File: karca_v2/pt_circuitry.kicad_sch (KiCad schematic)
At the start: 12 parts, among them U10 TLV9304xD, U9 TLV9304xD

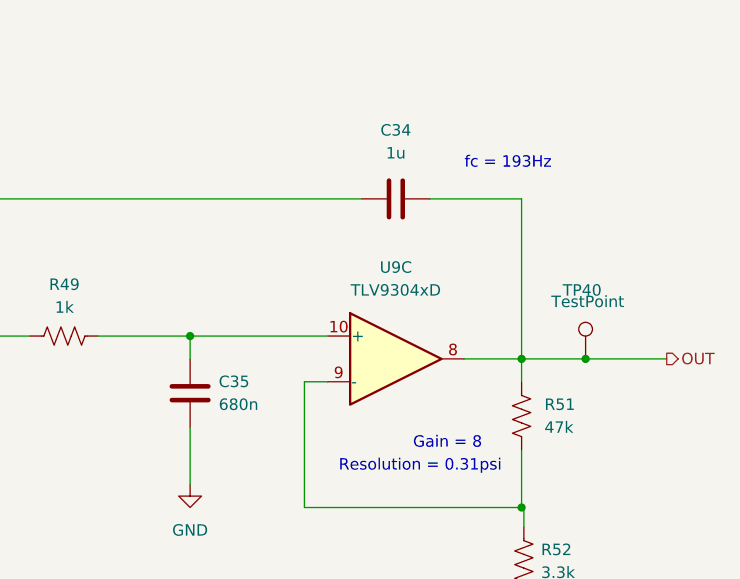
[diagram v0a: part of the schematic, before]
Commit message: swapped adcs
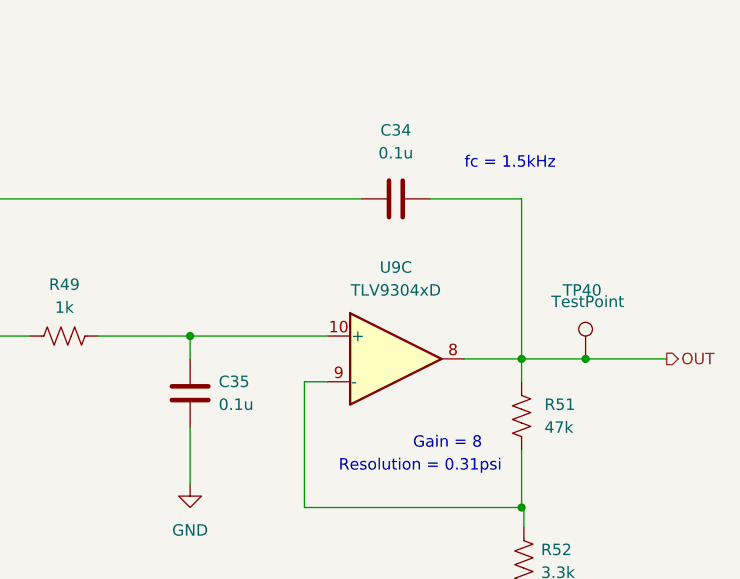
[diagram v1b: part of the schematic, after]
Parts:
- C34: value 1u -> 0.1u
- C35: value 680n -> 0.1u
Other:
- note added: "fc = 1.5kHz"
- note removed: "fc = 193Hz"
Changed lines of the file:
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@@
 	(title_block
 		(title "kARCA 2.0 Engine Control System")
-		(date "2026-03-23")
-		(rev "1.2")
+		(date "2024-12-16")
+		(rev "1.1")
 		(company "Rice Eclipse")
 		(comment 1 "Designed by Deepak Narayan")
@@
 		)
 	)
-	(text "fc = 193Hz\n"
+	(text "fc = 1.5kHz\n"
 		(exclude_from_sim no)
 		(at 199.136 54.991 0)
@@
 			)
 		)
-		(property "Value" "1u"
+		(property "Value" "0.1u"
 			(at 191.516 53.086 90)
 			(effects
@@
 			)
 		)
-		(property "Value" "680n"
+		(property "Value" "0.1u"
 			(at 171.831 81.026 0)
 			(effects

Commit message: All tests passed. Going to run DFM next
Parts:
- C34: value 0.1u -> 1u
- C35: value 0.1u -> 680n
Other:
- note added: "fc = 193Hz"
- note removed: "fc = 1.5kHz"
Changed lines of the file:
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@@
 	(title_block
 		(title "kARCA 2.0 Engine Control System")
-		(date "2024-12-16")
+		(date "2026-03-25")
 		(rev "1.1")
 		(company "Rice Eclipse")
@@
 		)
 	)
-	(text "fc = 1.5kHz\n"
+	(text "fc = 193Hz\n"
 		(exclude_from_sim no)
 		(at 199.136 54.991 0)
@@
 			)
 		)
-		(property "Value" "0.1u"
+		(property "Value" "1u"
 			(at 191.516 53.086 90)
 			(effects
@@
 			)
 		)
-		(property "Value" "0.1u"
+		(property "Value" "680n"
 			(at 171.831 81.026 0)
 			(effects

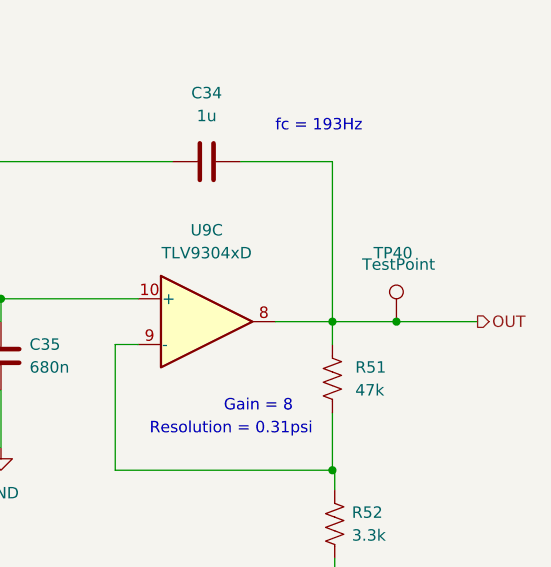
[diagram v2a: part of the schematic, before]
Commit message: fixed all routing. Now need to clean up vias
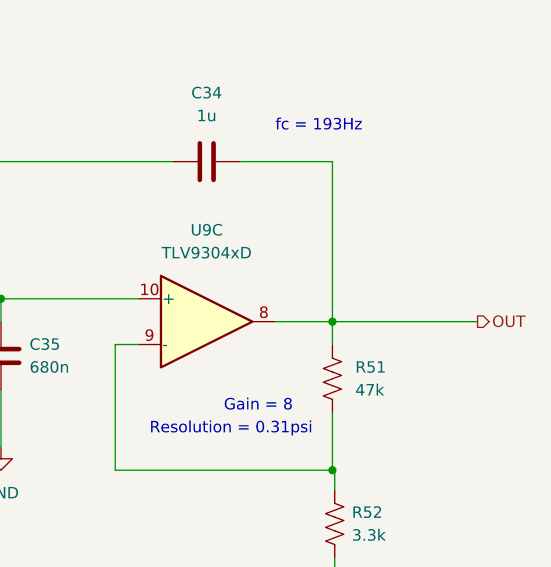
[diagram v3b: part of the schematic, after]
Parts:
- removed TP40: TestPoint, TestPoint:TestPoint_Pad_D2.0mm, symbol Connector:TestPoint
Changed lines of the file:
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@@
-	)
-	(junction
-		(at 212.598 75.946)
-		(diameter 0)
-		(color 0 0 0 0)
 	)
 	(junction
@@
 	(wire
 		(pts
-			(xy 205.486 75.946) (xy 212.598 75.946)
+			(xy 205.486 75.946) (xy 221.615 75.946)
 		)
 		(stroke
@@
 		(pts
 			(xy 106.426 70.866) (xy 86.106 70.866)
-		)
-		(stroke
-			(width 0)
-			(type default)
-		)
-	)
-	(wire
-		(pts
-			(xy 212.598 75.946) (xy 221.615 75.946)
 		)
 		(stroke
@@
 					(unit 1)
 				)
-			)
-		)
-	)
-	(symbol
-		(lib_id "Connector:TestPoint")
-		(at 212.598 75.946 0)
-		(unit 1)
-		(exclude_from_sim no)
-		(in_bom yes)
-		(on_board yes)
-		(dnp no)
-		(property "Reference" "TP40"
-			(at 210.058 68.326 0)
-			(effects
-				(font
-					(size 1.27 1.27)
-				)
-				(justify left)
-			)
-		)
-		(property "Value" "TestPoint"
-			(at 208.788 69.596 0)
-			(effects
-				(font
-					(size 1.27 1.27)
-				)
-				(justify left)
-			)
-		)
-		(property "Footprint" "TestPoint:TestPoint_Pad_D2.0mm"
-			(at 217.678 75.946 0)
-			(effects
-				(font
-					(size 1.27 1.27)
-				)
-				(hide yes)
-			)
-		)
-		(property "Datasheet" "~"
-			(at 217.678 75.946 0)
-			(effects
-				(font
-					(size 1.27 1.27)
-				)
-				(hide yes)
-			)
-		)
-		(property "Description" ""
-			(at 212.598 75.946 0)
-			(effects
-				(font
-					(size 1.27 1.27)
-				)
-				(hide yes)
-			)
-		)
-		(pin "1"
-		)
-		(instances
-			(project "karca_v2"
-				(path "/29cf4797-56f2-4f57-ae95-7df639362e3c/c566ee8f-cb19-4e44-a9af-dd67a0aa158e/044bcd6a-880d-4ffc-be8b-a03d76768183"
-					(reference "TP40")
-					(unit 1)
-				)
-				(path "/29cf4797-56f2-4f57-ae95-7df639362e3c/c566ee8f-cb19-4e44-a9af-dd67a0aa158e/60027281-032f-4987-83fe-1472a08d0df6"
-					(reference "TP49")
-					(unit 1)
-				)
-				(path "/29cf4797-56f2-4f57-ae95-7df639362e3c/c566ee8f-cb19-4e44-a9af-dd67a0aa158e/691cd68e-b9d2-4323-a044-22fc45a3ad38"
-					(reference "TP42")
-					(unit 1)
-				)
-				(path "/29cf4797-56f2-4f57-ae95-7df639362e3c/c566ee8f-cb19-4e44-a9af-dd67a0aa158e/c6078a97-3f1f-4f19-8ed7-752ec56dbc3c"
-					(reference "TP44")
-					(unit 1)
-				)

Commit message: final production version
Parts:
- R50: MPN (none) -> C17886
- R51: MPN (none) -> C25664
- R52: MPN (none) -> C26032
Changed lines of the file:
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@@
+			)
+		)
+		(property "MPN" "C25664"
+			(at 205.486 82.296 0)
+			(effects
+				(font
+					(size 1.27 1.27)
+				)
+				(hide yes)
 			)
 		)
@@
 			)
 		)
+		(property "MPN" "C17886"
+			(at 86.106 74.676 0)
+			(effects
+				(font
+					(size 1.27 1.27)
+				)
+				(hide yes)
+			)
+		)
 		(pin "1"
 		)
@@
 			(at 205.74 98.425 0)
 			(effects
+				(font
+					(size 1.27 1.27)
+				)
+				(hide yes)
+			)
+		)
+		(property "MPN" "C26032"
+			(at 205.74 98.425 0)
+			(effects
